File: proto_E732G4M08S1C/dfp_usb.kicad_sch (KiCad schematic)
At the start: 1 part, among them J1 USB_C_Receptacle_USB2.0_16P

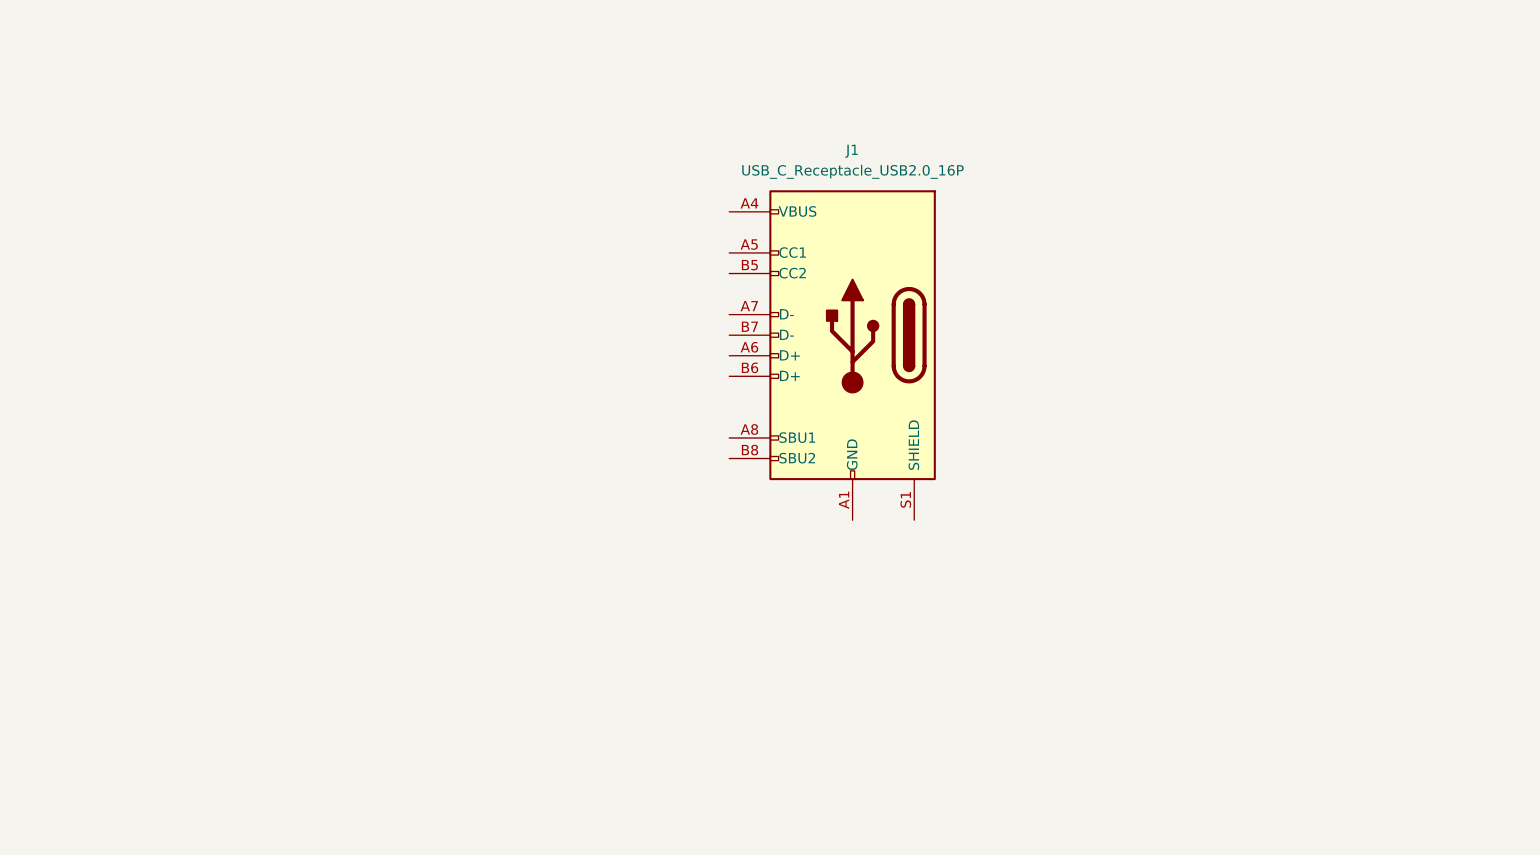
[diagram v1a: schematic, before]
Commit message: chg(pcb) more MCU and usb
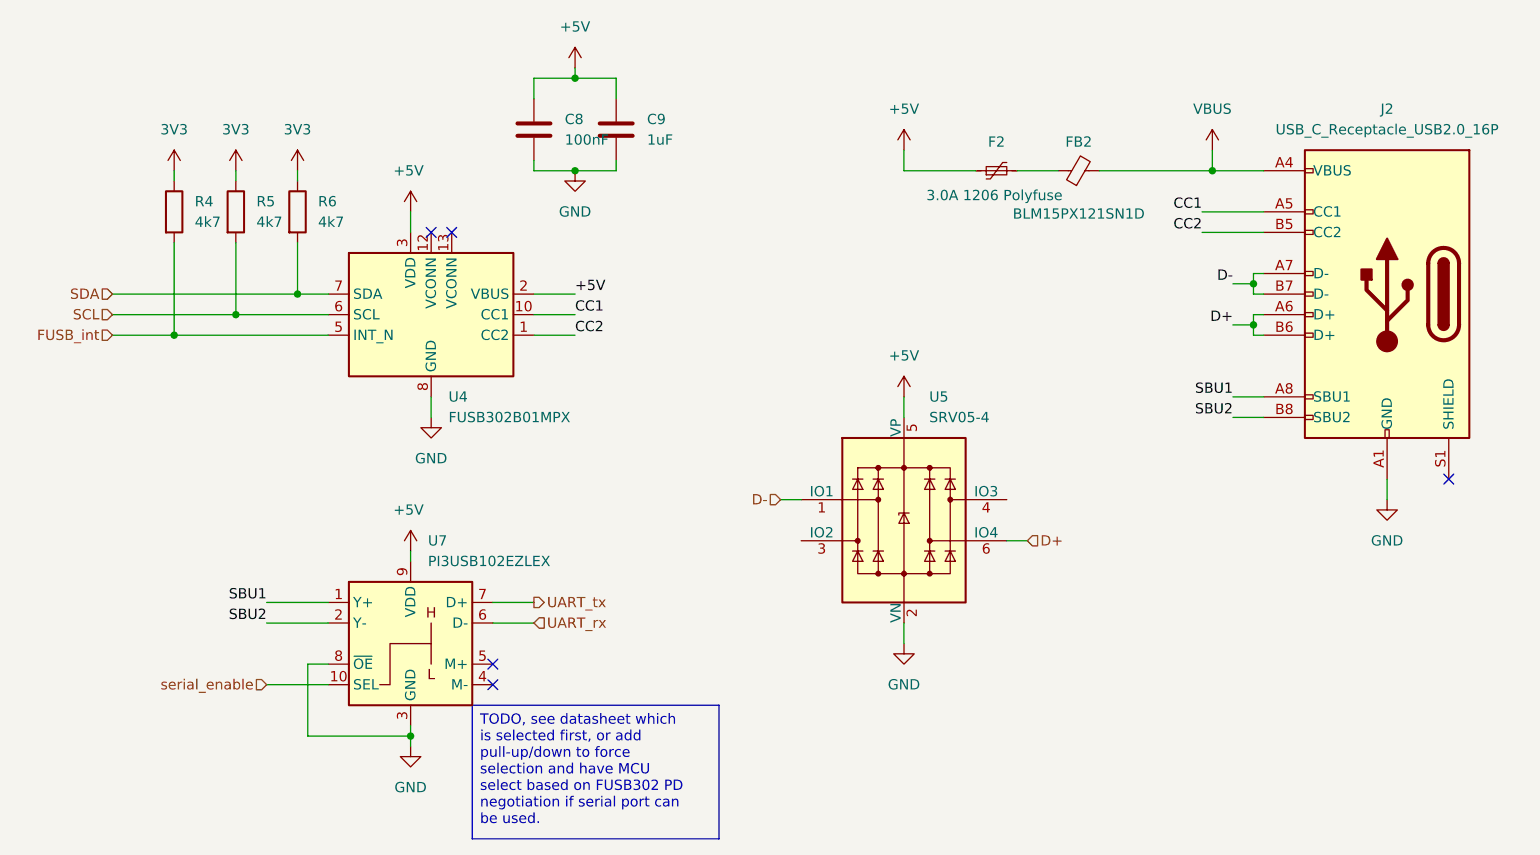
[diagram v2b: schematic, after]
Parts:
- removed J1: USB_C_Receptacle_USB2.0_16P, symbol Connector:USB_C_Receptacle_USB2.0_16P
- added C8: 100nF, Capacitor_SMD:C_0603_1608Metric, symbol Device:C
- added C9: 1uF, Capacitor_SMD:C_0603_1608Metric, symbol Device:C
- added F2: 3.0A 1206 Polyfuse, Fuse:Fuse_1206_3216Metric, symbol Device:Polyfuse_Small
- added FB2: BLM15PX121SN1D, Inductor_SMD:L_0402_1005Metric, symbol Device:FerriteBead_Small
- added J2: USB_C_Receptacle_USB2.0_16P, stellar:USB4510031A, symbol Connector:USB_C_Receptacle_USB2.0_16P
- added R4, R5, R6: 4k7, Resistor_SMD:R_0603_1608Metric, symbol Device:R
- added U4: FUSB302B01MPX, Package_DFN_QFN:WQFN-14-1EP_2.5x2.5mm_P0.5mm_EP1.45x1.45mm, symbol Interface_USB:FUSB302B01MPX
- added U5: SRV05-4, Package_TO_SOT_SMD:SOT-23-6, symbol Power_Protection:SRV05-4
- added U7: PI3USB102EZLEX, Package_DFN_QFN:UQFN-10_1.3x1.8mm_P0.4mm, symbol PCM_marbastlib-various:PI3USB102EZLEX
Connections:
- new net: F2.2, FB2.1
- new net +5V: C8.1, C9.1, F2.1, U4.2 (VBUS), U4.3 (VDD), U4.4 (VDD), U5.5 (VP), U7.9 (VDD)
- new net 3V3: R4.1, R5.1, R6.1
- new net CC1: J2.A5 (CC1), U4.10 (CC1), U4.11 (CC1)
- new net CC2: J2.B5 (CC2), U4.1 (CC2), U4.14 (CC2)
- new net D+: J2.A6 (D+), J2.B6 (D+), U5.6 (IO4)
- new net D-: J2.A7 (D-), J2.B7 (D-), U5.1 (IO1)
- new net FUSB_int: R4.2, U4.5 (INT_N)
- new net GND: C8.2, C9.2, J2.A1 (GND), J2.A12 (GND), J2.B1 (GND), J2.B12 (GND), U4.15 (GND), U4.8 (GND), U4.9 (GND), U5.2 (VN), U7.3 (GND), U7.8 (~{OE})
- new net SBU1: J2.A8 (SBU1), U7.1 (Y+)
- new net SBU2: J2.B8 (SBU2), U7.2 (Y-)
- new net SCL: R5.2, U4.6 (SCL)
- new net SDA: R6.2, U4.7 (SDA)
- new net UART_rx: U7.6 (D-)
- new net UART_tx: U7.7 (D+)
- new net VBUS: FB2.2, J2.A4 (VBUS), J2.A9 (VBUS), J2.B4 (VBUS), J2.B9 (VBUS)
- new net serial_enable: U7.10 (SEL)
- no-connect marks 0 -> 5

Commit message: feat(pcb) more changes
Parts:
- added C13: 100nF, Capacitor_SMD:C_0603_1608Metric, symbol Device:C
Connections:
- net +5V: now also C13.1
- net GND: now also C13.2
- net 3V3 renamed +3.3V
- no-connect marks 5 -> 7
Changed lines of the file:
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@@
+	)
+	(no_connect
+		(at 170.18 114.3)
 	)
 	(no_connect
@@
 	)
 	(no_connect
+		(at 144.78 119.38)
+	)
+	(no_connect
 		(at 101.6 81.28)
 	)
@@
 	(wire
 		(pts
+			(xy 67.31 123.19) (xy 67.31 124.46)
+		)
+		(stroke
+			(width 0)
+			(type default)
+		)
+	)
+	(wire
+		(pts
 			(xy 82.55 88.9) (xy 86.36 88.9)
 		)
@@
 		(pts
 			(xy 121.92 72.39) (xy 121.92 73.66)
+		)
+		(stroke
+			(width 0)
+			(type default)
+		)
+	)
+	(wire
+		(pts
+			(xy 67.31 114.3) (xy 67.31 115.57)
 		)
 		(stroke
@@
 	)
 	(hierarchical_label "D-"
-		(shape input)
+		(shape bidirectional)
 		(at 142.24 114.3 180)
 		(effects
@@
 	)
 	(hierarchical_label "D+"
-		(shape input)
+		(shape bidirectional)
 		(at 172.72 119.38 0)
 		(effects
@@
 	)
 	(symbol
+		(lib_id "power:VCC")
+		(at 67.31 114.3 0)
+		(unit 1)
+		(exclude_from_sim no)
+		(in_bom yes)
+		(on_board yes)
+		(dnp no)
+		(fields_autoplaced yes)
+		(property "Reference" "#PWR060"
+			(at 67.31 118.11 0)
+			(effects
+				(font
+					(size 1.27 1.27)
+				)
+				(hide yes)
+			)
+		)
+		(property "Value" "+5V"
+			(at 67.31 109.22 0)
+			(effects
+				(font
+					(size 1.27 1.27)
+				)
+			)
+		)
+		(property "Footprint" ""
+			(at 67.31 114.3 0)
+			(effects
+				(font
+					(size 1.27 1.27)
+				)
+				(hide yes)
+			)
+		)
+		(property "Datasheet" ""
+			(at 67.31 114.3 0)
+			(effects
+				(font
+					(size 1.27 1.27)
+				)
+				(hide yes)
+			)
+		)
+		(property "Description" "Power symbol creates a global label with name \"VCC\""
+			(at 67.31 114.3 0)
+			(effects
+				(font
+					(size 1.27 1.27)
+				)
+				(hide yes)
+			)
+		)
+		(pin "1"
+		)
+		(instances
+			(project "proto_E732G4M08S1C"
+				(path "/3062eac5-ad35-4bd4-9fe0-12754d69cac0/ff56f265-b553-4371-8036-b8b3fc4fb93a"
+					(reference "#PWR060")
+					(unit 1)
+				)
+			)
+		)
+	)
+	(symbol
 		(lib_id "Power_Protection:SRV05-4")
 		(at 157.48 116.84 0)
@@
 			)
 		)
-		(property "Value" "3V3"
+		(property "Value" "+3.3V"
 			(at 67.31 68.58 0)
 			(effects
@@
 		(on_board yes)
 		(dnp no)
-		(fields_autoplaced yes)
 		(property "Reference" "C8"
-			(at 115.57 67.3099 0)
+			(at 105.664 67.564 0)
 			(effects
 				(font
@@
 		)
 		(property "Value" "100nF"
-			(at 115.57 69.8499 0)
+			(at 102.362 69.85 0)
 			(effects
 				(font
@@
 			)
 		)
-		(property "Value" "3V3"
+		(property "Value" "+3.3V"
 			(at 82.55 68.58 0)
 			(effects
@@
 			)
 		)
-		(property "Value" "3V3"
+		(property "Value" "+3.3V"
 			(at 74.93 68.58 0)
 			(effects
@@
 					(unit 1)
 				)
+			)
+		)
+	)
+	(symbol
+		(lib_id "power:GND")
+		(at 67.31 124.46 0)
+		(unit 1)
+		(exclude_from_sim no)
+		(in_bom yes)
+		(on_board yes)
+		(dnp no)
+		(fields_autoplaced yes)
+		(property "Reference" "#PWR061"
+			(at 67.31 130.81 0)
+			(effects
+				(font
+					(size 1.27 1.27)
+				)
+				(hide yes)
+			)
+		)
+		(property "Value" "GND"
+			(at 67.31 129.54 0)
+			(effects
+				(font
+					(size 1.27 1.27)
+				)
+			)
+		)
+		(property "Footprint" ""
+			(at 67.31 124.46 0)
+			(effects
+				(font
+					(size 1.27 1.27)
+				)
+				(hide yes)
+			)
+		)
+		(property "Datasheet" ""
+			(at 67.31 124.46 0)
+			(effects
+				(font
+					(size 1.27 1.27)
+				)
+				(hide yes)
+			)
+		)
+		(property "Description" "Power symbol creates a global label with name \"GND\" , ground"
+			(at 67.31 124.46 0)
+			(effects
+				(font
+					(size 1.27 1.27)
+				)
+				(hide yes)
+			)
+		)
+		(pin "1"
+		)
+		(instances
+			(project "proto_E732G4M08S1C"
+				(path "/3062eac5-ad35-4bd4-9fe0-12754d69cac0/ff56f265-b553-4371-8036-b8b3fc4fb93a"
+					(reference "#PWR061")
+					(unit 1)
+				)
+			)
+		)
+	)
+	(symbol
+		(lib_id "Device:C")
+		(at 67.31 119.38 0)
+		(unit 1)
+		(exclude_from_sim no)
+		(in_bom yes)
+		(on_board yes)
+		(dnp no)
+		(fields_autoplaced yes)
+		(property "Reference" "C13"
+			(at 71.12 118.1099 0)
+			(effects
+				(font
+					(size 1.27 1.27)
+				)
+				(justify left)
+			)
+		)
+		(property "Value" "100nF"
+			(at 71.12 120.6499 0)
+			(effects
+				(font
+					(size 1.27 1.27)
+				)
+				(justify left)
+			)
+		)
+		(property "Footprint" "Capacitor_SMD:C_0603_1608Metric"
+			(at 68.2752 123.19 0)
+			(effects
+				(font
+					(size 1.27 1.27)
+				)
+				(hide yes)
+			)
+		)
+		(property "Datasheet" "~"
+			(at 67.31 119.38 0)
+			(effects
+				(font
+					(size 1.27 1.27)
+				)
+				(hide yes)
+			)
+		)
+		(property "Description" "Unpolarized capacitor"
+			(at 67.31 119.38 0)
+			(effects
+				(font
+					(size 1.27 1.27)
+				)
+				(hide yes)
+			)
+		)
+		(pin "2"
+		)
+		(pin "1"
+		)
+		(instances
+			(project "proto_E732G4M08S1C"
+				(path "/3062eac5-ad35-4bd4-9fe0-12754d69cac0/ff56f265-b553-4371-8036-b8b3fc4fb93a"
+					(reference "C13")
+					(unit 1)
+				)
